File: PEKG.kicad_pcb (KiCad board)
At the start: 2 copper layers, 90 x 45 mm, 100 parts, among them J1 USB_C_Receptacle, J2 AudioJack3, U1 TL072, U10 74LVC1G125, U11 74LVC1G125, U12 NCS21802DMR2G, U13 NCS21802DMR2G, U2 TL072, U3 INA350CDSIDDFR, U4 74LVC2G74, U5 TS5A63157DBV, U6 TS5A63157DBV, U7 TS5A63157DBV, U8 NCS21802DMR2G, U9 74LVC1G125

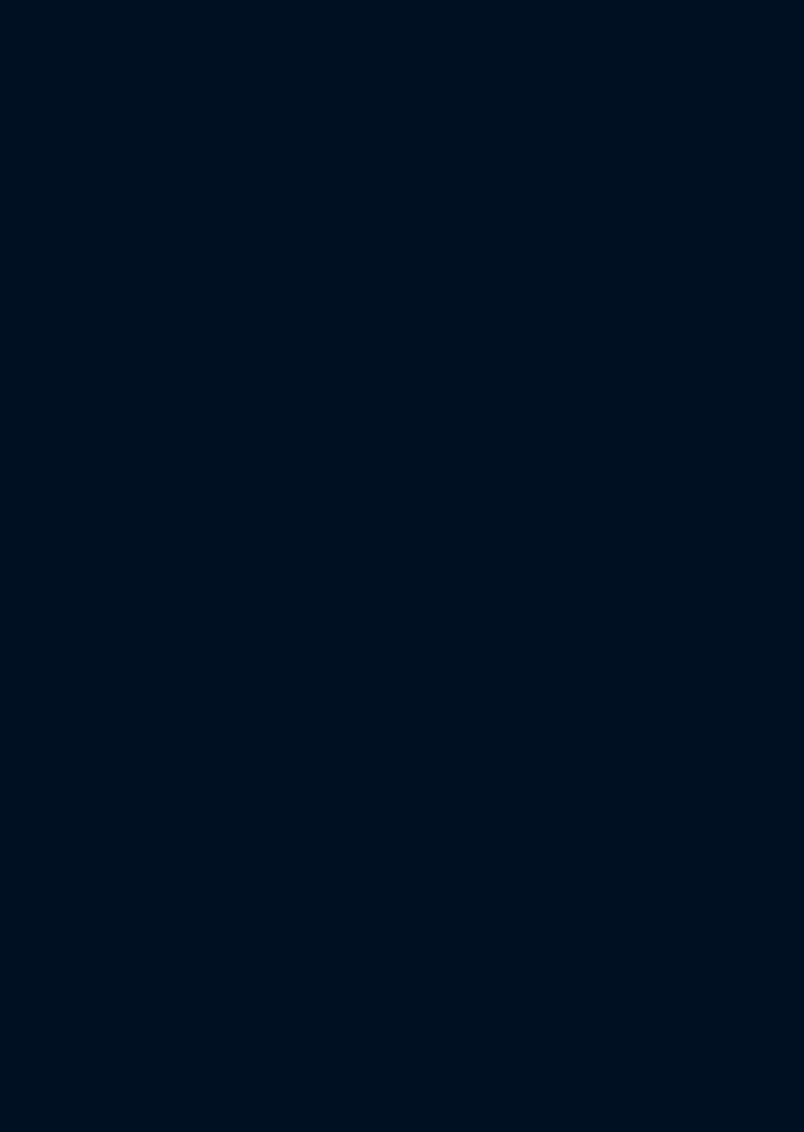
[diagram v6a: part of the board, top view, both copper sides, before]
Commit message: Added testpoints.
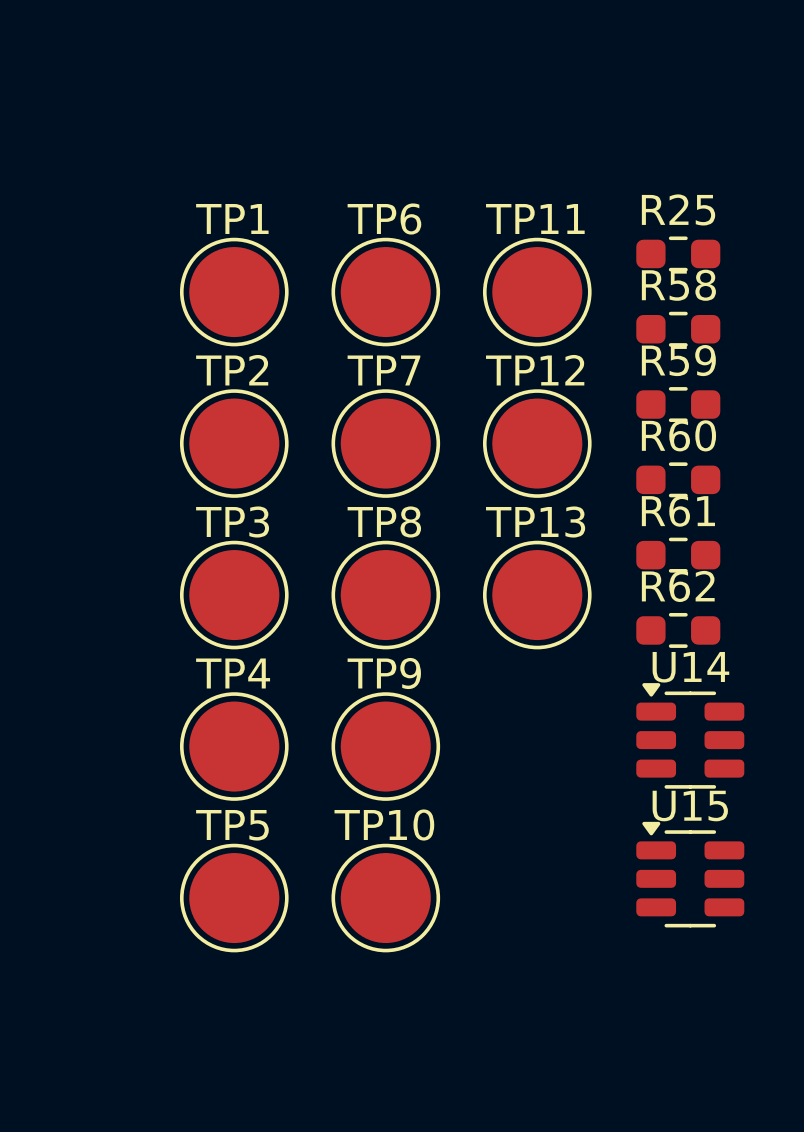
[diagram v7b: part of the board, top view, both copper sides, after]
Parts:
- added R25: 100k, Resistor_SMD:R_0603_1608Metric_Pad0.98x0.95mm_HandSolder, F.Cu at (217.8, 114.1)
- added R58: 330k, Resistor_SMD:R_0603_1608Metric_Pad0.98x0.95mm_HandSolder, F.Cu at (217.8, 116.6)
- added R59: 10Meg, Resistor_SMD:R_0603_1608Metric_Pad0.98x0.95mm_HandSolder, F.Cu at (217.8, 119.1)
- added R60: 1Meg, Resistor_SMD:R_0603_1608Metric_Pad0.98x0.95mm_HandSolder, F.Cu at (217.8, 121.7)
- added R61: 1Meg, Resistor_SMD:R_0603_1608Metric_Pad0.98x0.95mm_HandSolder, F.Cu at (217.8, 124.2)
- added R62: 1Meg, Resistor_SMD:R_0603_1608Metric_Pad0.98x0.95mm_HandSolder, F.Cu at (217.8, 126.7)
- added TP1: TestPoint, TestPoint:TestPoint_Pad_D3.0mm, F.Cu at (203.0, 115.4)
- added TP10: TestPoint, TestPoint:TestPoint_Pad_D3.0mm, F.Cu at (208.0, 135.6)
- added TP11: TestPoint, TestPoint:TestPoint_Pad_D3.0mm, F.Cu at (213.1, 115.4)
- added TP12: TestPoint, TestPoint:TestPoint_Pad_D3.0mm, F.Cu at (213.1, 120.4)
- added TP13: TestPoint, TestPoint:TestPoint_Pad_D3.0mm, F.Cu at (213.1, 125.5)
- added TP2: TestPoint, TestPoint:TestPoint_Pad_D3.0mm, F.Cu at (203.0, 120.4)
- added TP3: TestPoint, TestPoint:TestPoint_Pad_D3.0mm, F.Cu at (203.0, 125.5)
- added TP4: TestPoint, TestPoint:TestPoint_Pad_D3.0mm, F.Cu at (203.0, 130.5)
- added TP5: TestPoint, TestPoint:TestPoint_Pad_D3.0mm, F.Cu at (203.0, 135.6)
- added TP6: TestPoint, TestPoint:TestPoint_Pad_D3.0mm, F.Cu at (208.0, 115.4)
- added TP7: TestPoint, TestPoint:TestPoint_Pad_D3.0mm, F.Cu at (208.0, 120.4)
- added TP8: TestPoint, TestPoint:TestPoint_Pad_D3.0mm, F.Cu at (208.0, 125.5)
- added TP9: TestPoint, TestPoint:TestPoint_Pad_D3.0mm, F.Cu at (208.0, 130.5)
- added U14: TS5A63157DBV, Package_TO_SOT_SMD:SOT-23-6, F.Cu at (218.2, 130.3)
- added U15: TS5A63157DBV, Package_TO_SOT_SMD:SOT-23-6, F.Cu at (218.2, 134.9)
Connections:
- C16 pad 2: Net-(U1A-+) -> Net-(U1A--)
- C18 pad 1: Net-(U2A-+) -> Net-(U2A--)
- C19 pad 1: Net-(U2A--) -> FIL_OUT
- C20 pad 1: Net-(U2A--) -> FIL_OUT
- C24 pad 2: Net-(U2B-+) -> Net-(U2B--)
- C42 pad 1: GND -> VBUS
- C42 pad 2: VBUS -> GND
- JP6 pad 1: GAIN_5000_OUTPUT -> FIL_OUT
- R22 pad 2: SBU1 -> SBU1_T
- R26 pad 2: Net-(U1A-+) -> Net-(U1A--)
- R27 pad 1: Net-(U2B-+) -> Net-(U2B--)
- R30 pad 1: GAIN_5000_OUTPUT -> FIL_OUT
- R30 pad 2: Net-(U2B--) -> Net-(U2B-+)
- R31 pad 2: Net-(U2B--) -> Net-(U2B-+)
- R34 pad 1: Net-(U2A-+) -> Net-(U2A--)
- R36 pad 1: Net-(U2A--) -> FIL_OUT
- R38 pad 1: Net-(U2A-+) -> Net-(U2A--)
- R39 pad 1: Net-(U2A--) -> FIL_OUT
- R40 pad 1: Net-(U2A--) -> FIL_OUT
- R47 pad 2: Net-(U2B-+) -> Net-(U2B--)
- R48 pad 2: Net-(U2B-+) -> Net-(U2B--)
- R51 pad 1: Net-(U1A-+) -> Net-(U1A--)
- R56 pad 1: Net-(U2A--) -> FIL_OUT
- U1 pad 2: GAIN_500_OUTPUT -> Net-(U1A--)
- U1 pad 3: Net-(U1A-+) -> GAIN_500_OUTPUT
- U2 pad 3: Net-(U2A-+) -> 2.5V
- U5 pad 1: SENSED_DIR -> LEVELED_OUTPUT
- U5 pad 4: SBU1 -> SBU1_A
- U6 pad 3: SENSED_DIR -> LEVELED_OUTPUT
- U6 pad 4: SBU2 -> SBU2_A
- U9 pad 2: SBU1 -> SBU1_T

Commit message: dsf
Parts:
- removed C25: 10u, Capacitor_SMD:C_0603_1608Metric_Pad1.08x0.95mm_HandSolder
- removed C35, C36, C37, C38, C39, C40: 100n, Capacitor_SMD:C_0603_1608Metric_Pad1.08x0.95mm_HandSolder
- removed R19, R20, R21, R22, R25: 100k, Resistor_SMD:R_0603_1608Metric_Pad0.98x0.95mm_HandSolder
- removed TP12, TP13: TestPoint, TestPoint:TestPoint_Pad_D3.0mm
- removed U10, U11, U9: 74LVC1G125, Package_TO_SOT_SMD:SOT-23-5_HandSoldering
- removed U14, U15, U5, U6: TS5A63157DBV, Package_TO_SOT_SMD:SOT-23-6
- removed U4: 74LVC2G74, Package_SO:VSSOP-8_2.3x2mm_P0.5mm
- added BT1: Battery_Cell, Battery:BatteryHolder_Keystone_2462_2xAA, B.Cu at (117.2, 129.1)
- added C22: 1u, Resistor_SMD:R_0603_1608Metric_Pad0.98x0.95mm_HandSolder, F.Cu at (156.5, 162.2)
- added C47: 10u, Resistor_SMD:R_1206_3216Metric_Pad1.30x1.75mm_HandSolder, F.Cu at (143.3, 156.8)
- added C48: 10u, Resistor_SMD:R_1206_3216Metric_Pad1.30x1.75mm_HandSolder, F.Cu at (143.3, 160.1)
- added JP7: Jumper_2_Bridged, Jumper:SolderJumper-2_P1.3mm_Bridged_RoundedPad1.0x1.5mm, F.Cu at (157.5, 153.7)
- added JP8: Jumper_2_Open, Jumper:SolderJumper-2_P1.3mm_Open_RoundedPad1.0x1.5mm, F.Cu at (157.5, 157.2)
- added L2: 4.7u, Inductor_THT:L_Radial_D7.5mm_P3.50mm_Fastron_07P, F.Cu at (149.0, 156.4)
- added L3: 4.7u, Inductor_SMD:L_Bourns_SRN6045TA, F.Cu at (150.3, 164.7)
- added R63: 10k, Resistor_SMD:R_0603_1608Metric_Pad0.98x0.95mm_HandSolder, F.Cu at (156.5, 167.2)
- C41: value 100n -> 10u; footprint Capacitor_SMD:C_0603_1608Metric_Pad1.08x0.95mm_HandSolder -> Resistor_SMD:R_1206_3216Metric_Pad1.30x1.75mm_HandSolder
- J1: value USB_C_Receptacle -> AudioJack4; footprint Connector_USB:USB_C_Receptacle_Amphenol_12401610E4-2A_CircularHoles -> Connector_Audio:Jack_3.5mm_CUI_SJ1-3524N_Horizontal
- R62: value 1Meg -> 10k
- U7: value TS5A63157DBV -> TLV61070ADBVR
- moved R62 72.1 mm to (156.5, 164.7)
- moved U7 43.7 mm to (142.9, 164.1), turned to 0 degrees
- moved C41 33.0 mm to (143.3, 153.5), turned to 0 degrees
- moved J1 1.10 mm to (185.6, 122.5)
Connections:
- C41 pad 1: GND -> Earth
- C41 pad 2: VBUS -> Net-(JP8-A)
- R62 pad 1: Net-(C38-Pad2) -> Net-(U7-FB)
- R62 pad 2: GND -> Net-(JP8-A)
- U7 pad 1: VBUS -> Net-(U7-SW)
- U7 pad 2: GND -> Earth
- U7 pad 3: GND -> Net-(U7-EN)
- U7 pad 4: Net-(U4-C) -> Net-(U7-FB)
- U7 pad 5: VBUS -> Net-(JP8-A)
- U7 pad 6: EN -> Net-(U7-EN)
